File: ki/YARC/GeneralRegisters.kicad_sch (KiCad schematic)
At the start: 12 parts, among them U71 74LS670, U72 74LS670, U73 74LS157, U74 74LS670, U75 74LS670, U76 74LS157, U77 74LS670, U78 74LS670, U79 74LS157, U80 74LS670, U81 74LS670, U82 74LS157

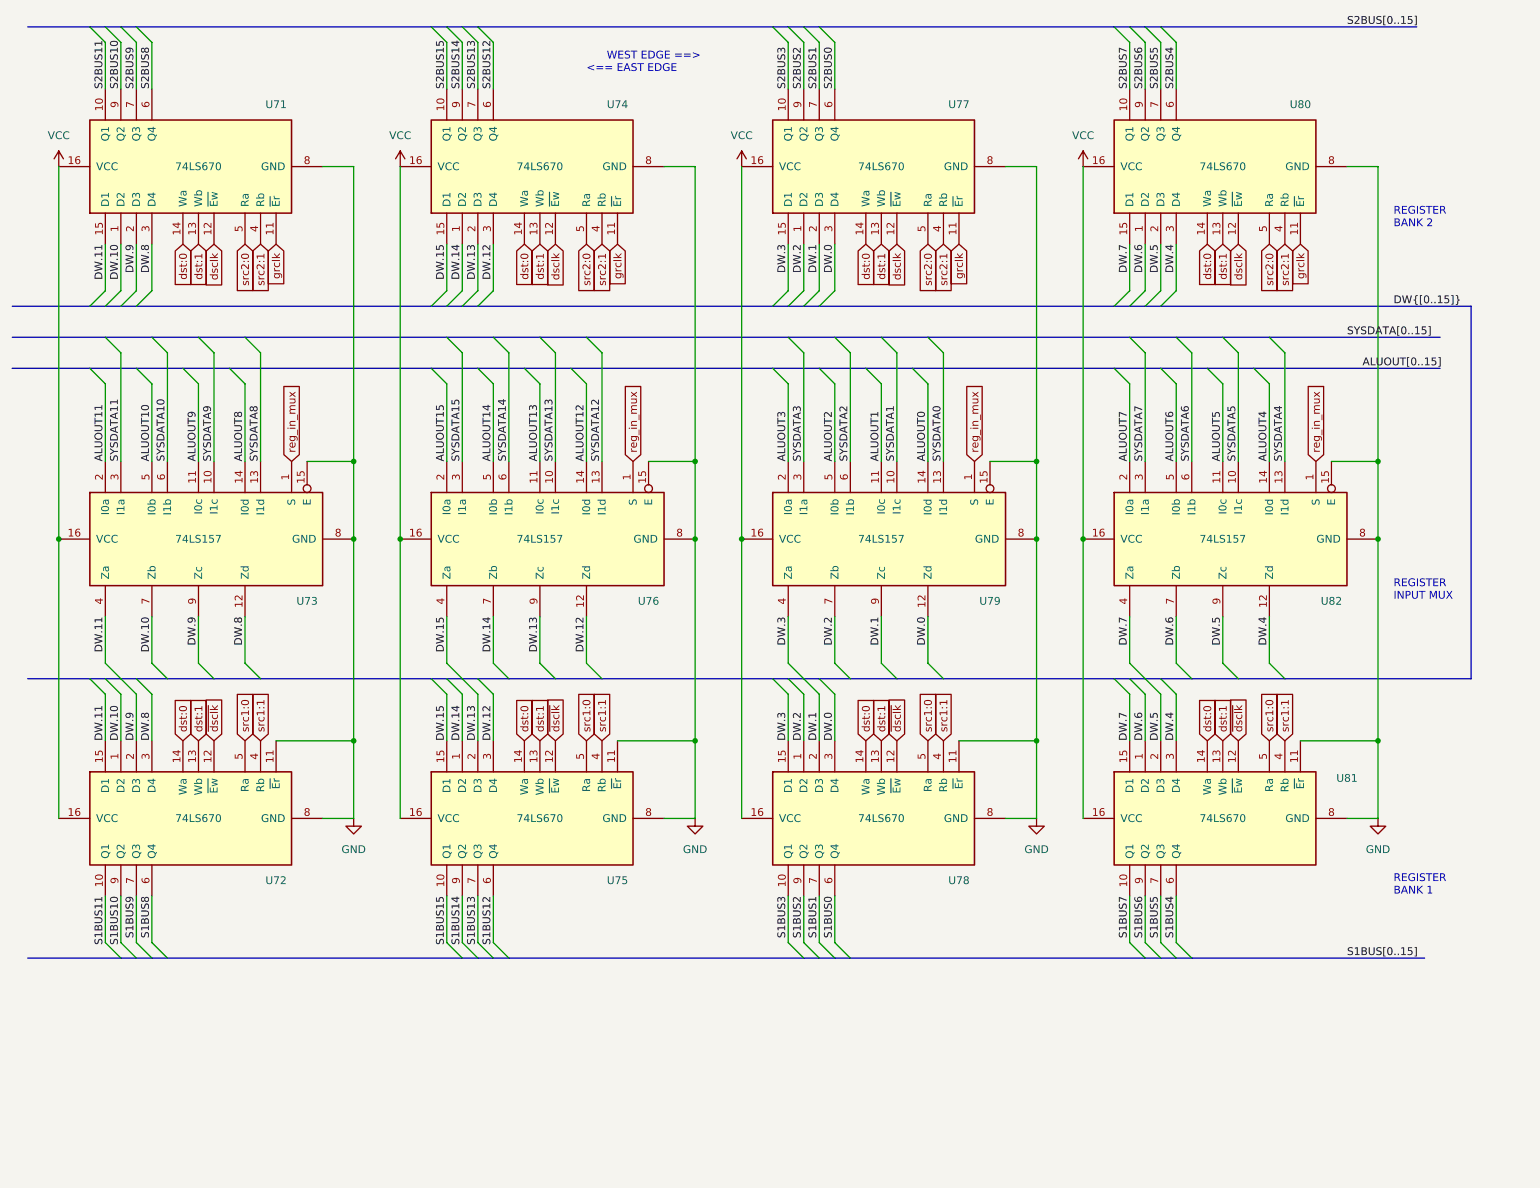
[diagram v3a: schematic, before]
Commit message: Add delay line for general register write signal. Minor corrections and cleanups.
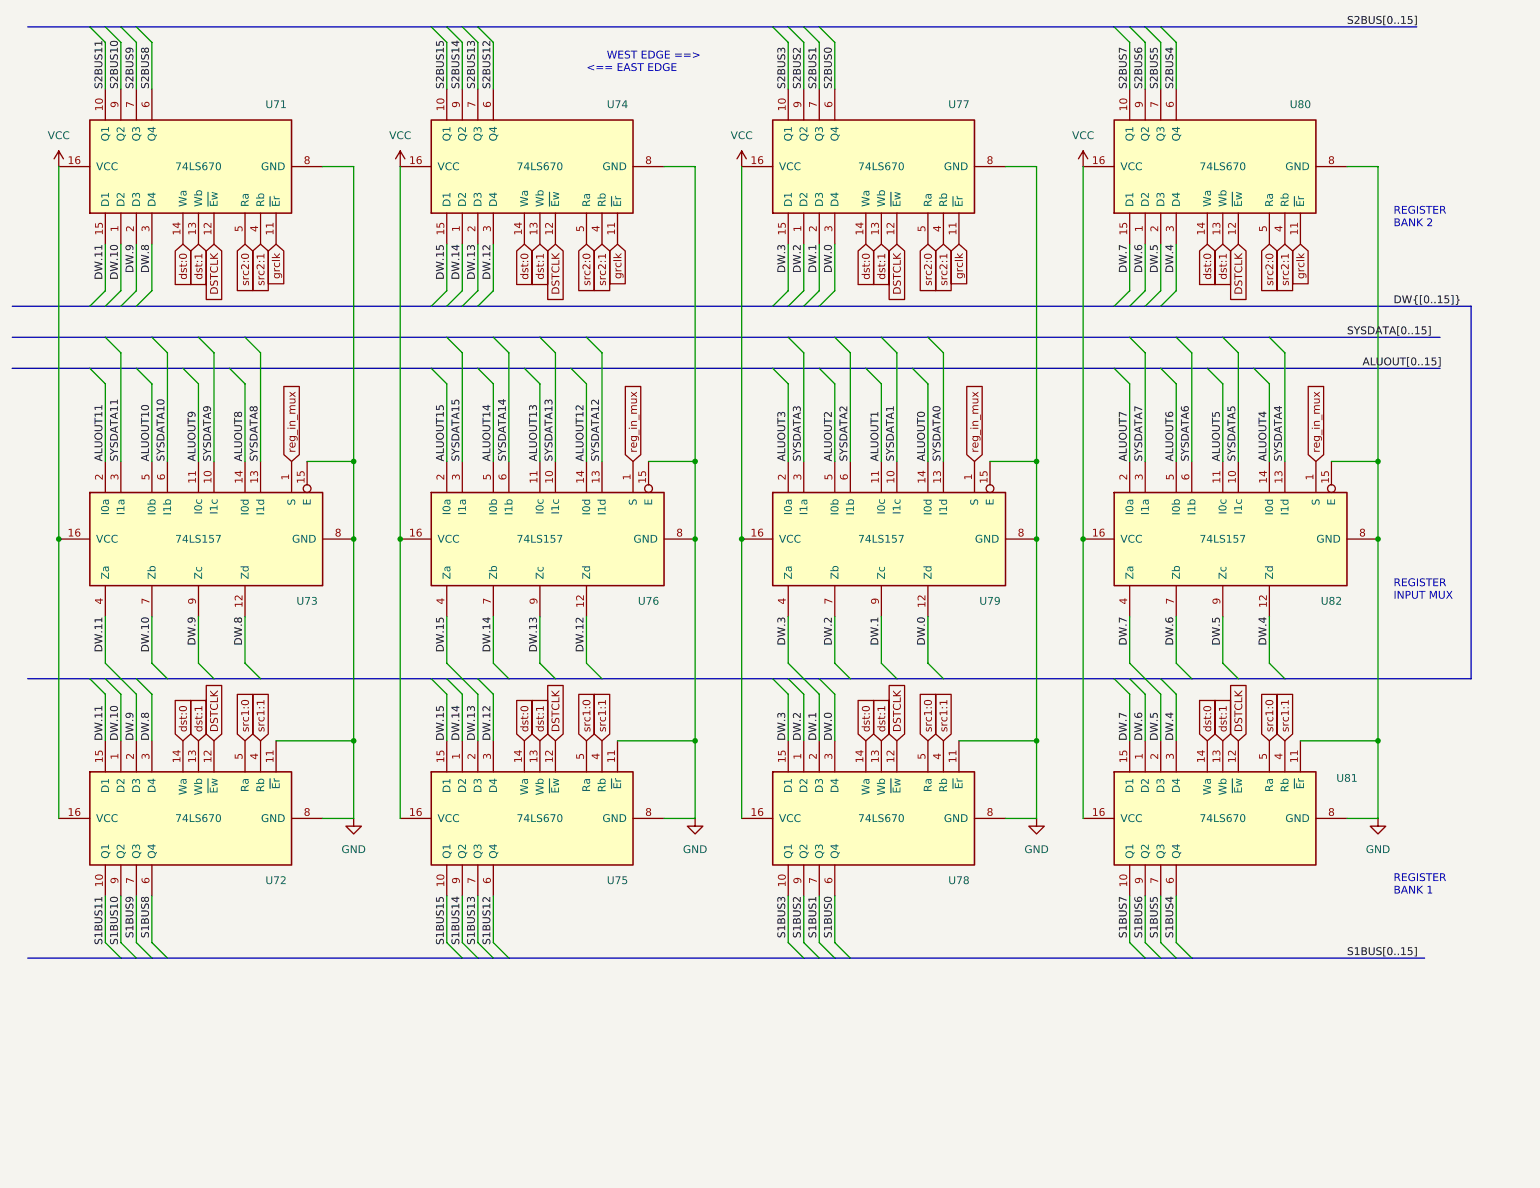
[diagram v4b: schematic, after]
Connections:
- net ~{dsclk} is gone; now on net DSTCLK: U72.12 (~{Ew}), U75.12 (~{Ew}), U78.12 (~{Ew}), U81.12 (~{Ew})
- net dsclk renamed DSTCLK
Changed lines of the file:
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@@
     )
   )
-  (global_label "~{dsclk}" (shape input) (at 104.14 132.08 90) (fields_autoplaced)
-    (effects (font (size 1.27 1.27)) (justify left))
-    (property "Intersheet References" "${INTERSHEET_REFS}" (id 0) (at 104.2194 124.7079 90)
+  (global_label "DSTCLK" (shape input) (at 104.14 132.08 90) (fields_autoplaced)
+    (effects (font (size 1.27 1.27)) (justify left))
+    (property "Intersheet References" "${INTERSHEET_REFS}" (id 0) (at 104.0606 122.6517 90)
       (effects (font (size 1.27 1.27)) (justify left) hide)
     )
@@
     )
   )
-  (global_label "dsclk" (shape input) (at 160.02 50.8 270) (fields_autoplaced)
-    (effects (font (size 1.27 1.27)) (justify right))
-    (property "Intersheet References" "${INTERSHEET_REFS}" (id 0) (at 159.9406 58.1721 90)
+  (global_label "DSTCLK" (shape input) (at 160.02 50.8 270) (fields_autoplaced)
+    (effects (font (size 1.27 1.27)) (justify right))
+    (property "Intersheet References" "${INTERSHEET_REFS}" (id 0) (at 159.9406 60.2283 90)
       (effects (font (size 1.27 1.27)) (justify right) hide)
     )
@@
     )
   )
-  (global_label "~{dsclk}" (shape input) (at 48.26 132.08 90) (fields_autoplaced)
-    (effects (font (size 1.27 1.27)) (justify left))
-    (property "Intersheet References" "${INTERSHEET_REFS}" (id 0) (at 48.3394 124.7079 90)
-      (effects (font (size 1.27 1.27)) (justify left) hide)
-    )
-  )
-  (global_label "dsclk" (shape input) (at 104.14 50.8 270) (fields_autoplaced)
-    (effects (font (size 1.27 1.27)) (justify right))
-    (property "Intersheet References" "${INTERSHEET_REFS}" (id 0) (at 104.0606 58.1721 90)
+  (global_label "DSTCLK" (shape input) (at 48.26 132.08 90) (fields_autoplaced)
+    (effects (font (size 1.27 1.27)) (justify left))
+    (property "Intersheet References" "${INTERSHEET_REFS}" (id 0) (at 48.1806 122.6517 90)
+      (effects (font (size 1.27 1.27)) (justify left) hide)
+    )
+  )
+  (global_label "DSTCLK" (shape input) (at 104.14 50.8 270) (fields_autoplaced)
+    (effects (font (size 1.27 1.27)) (justify right))
+    (property "Intersheet References" "${INTERSHEET_REFS}" (id 0) (at 104.0606 60.2283 90)
       (effects (font (size 1.27 1.27)) (justify right) hide)
     )
@@
     )
   )
-  (global_label "~{dsclk}" (shape input) (at 160.02 132.08 90) (fields_autoplaced)
-    (effects (font (size 1.27 1.27)) (justify left))
-    (property "Intersheet References" "${INTERSHEET_REFS}" (id 0) (at 160.0994 124.7079 90)
+  (global_label "DSTCLK" (shape input) (at 160.02 132.08 90) (fields_autoplaced)
+    (effects (font (size 1.27 1.27)) (justify left))
+    (property "Intersheet References" "${INTERSHEET_REFS}" (id 0) (at 159.9406 122.6517 90)
       (effects (font (size 1.27 1.27)) (justify left) hide)
     )
@@
     )
   )
-  (global_label "dsclk" (shape input) (at 215.9 50.8 270) (fields_autoplaced)
-    (effects (font (size 1.27 1.27)) (justify right))
-    (property "Intersheet References" "${INTERSHEET_REFS}" (id 0) (at 215.8206 58.1721 90)
+  (global_label "DSTCLK" (shape input) (at 215.9 50.8 270) (fields_autoplaced)
+    (effects (font (size 1.27 1.27)) (justify right))
+    (property "Intersheet References" "${INTERSHEET_REFS}" (id 0) (at 215.8206 60.2283 90)
       (effects (font (size 1.27 1.27)) (justify right) hide)
     )
@@
     )
   )
-  (global_label "dsclk" (shape input) (at 48.26 50.8 270) (fields_autoplaced)
-    (effects (font (size 1.27 1.27)) (justify right))
-    (property "Intersheet References" "${INTERSHEET_REFS}" (id 0) (at 48.1806 58.1721 90)
+  (global_label "DSTCLK" (shape input) (at 48.26 50.8 270) (fields_autoplaced)
+    (effects (font (size 1.27 1.27)) (justify right))
+    (property "Intersheet References" "${INTERSHEET_REFS}" (id 0) (at 48.1806 60.2283 90)
       (effects (font (size 1.27 1.27)) (justify right) hide)
     )
@@
     )
   )
-  (global_label "~{dsclk}" (shape input) (at 215.9 132.08 90) (fields_autoplaced)
-    (effects (font (size 1.27 1.27)) (justify left))
-    (property "Intersheet References" "${INTERSHEET_REFS}" (id 0) (at 215.9794 124.7079 90)
-      (effects (font (size 1.27 1.27)) (justify left) hide)
-    )
+  (global_label "DSTCLK" (shape input) (at 215.9 132.08 90) (fields_autoplaced)
+    (effects (font (size 1.27 1.27)) (justify left))
+    (property "Intersheet References" "${INTERSHEET_REFS}" (id 0) (at 215.8206 122.6517 90)
+      (effects (font (size 1.27 1.27)) (justify left) hide)
+    )

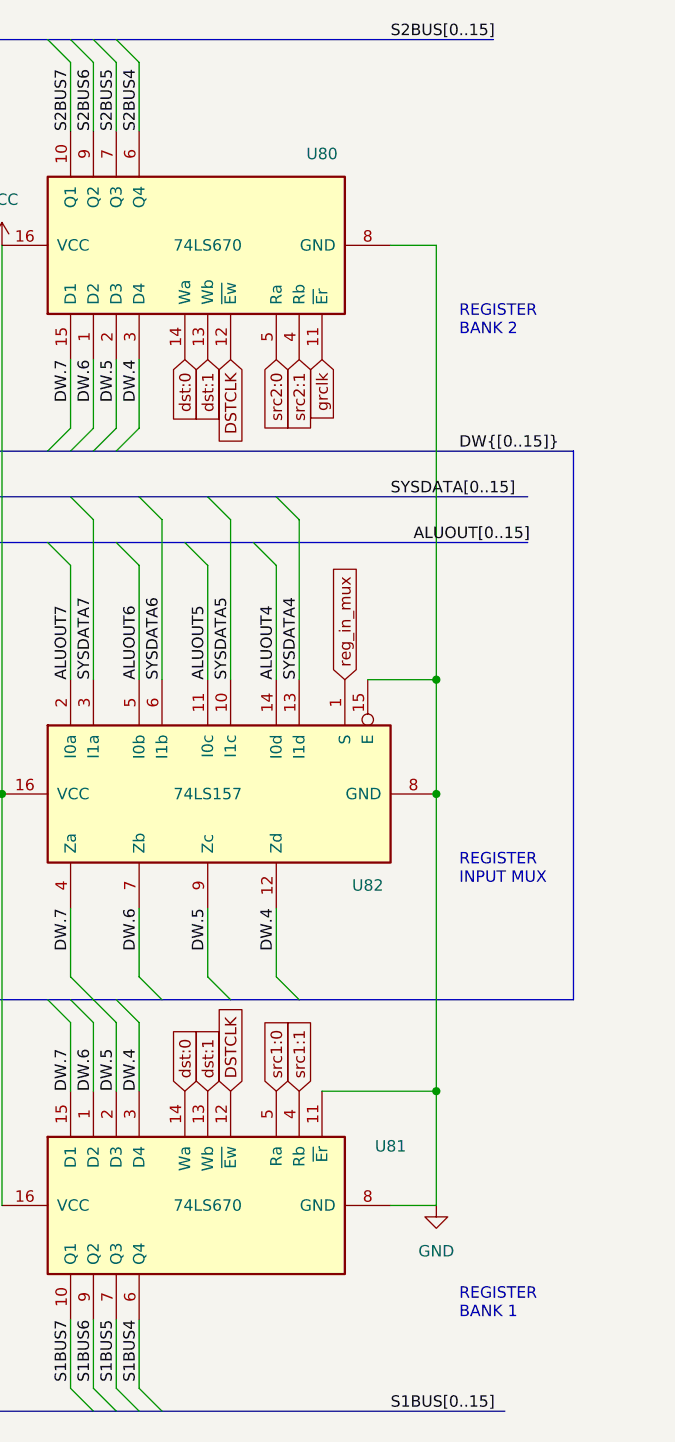
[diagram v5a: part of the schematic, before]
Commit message: Removed about 2/3 of 2300+ errors from the ERC
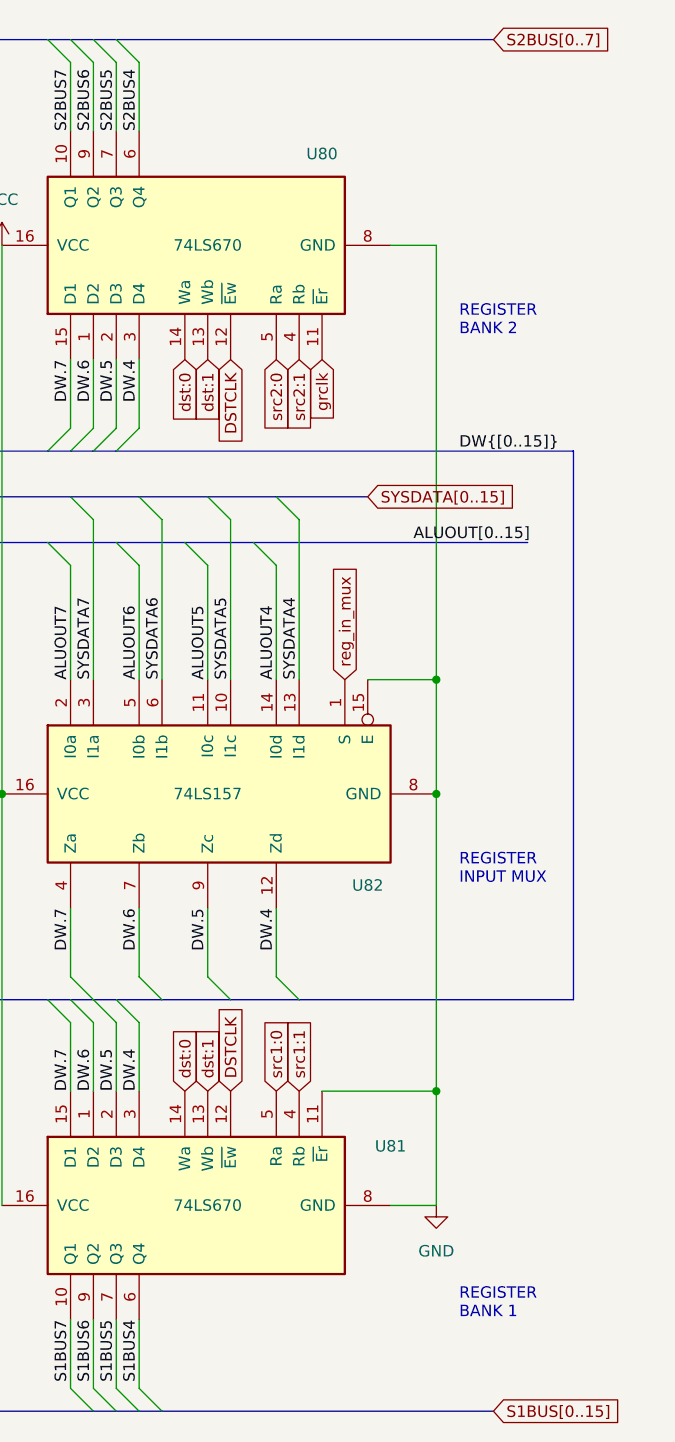
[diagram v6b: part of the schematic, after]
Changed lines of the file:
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@@
     (stroke (width 0) (type default))
   )
-  (bus (pts (xy 208.28 167.64) (xy 246.38 167.64))
+  (bus (pts (xy 208.28 167.64) (xy 245.11 167.64))
     (stroke (width 0) (type default))
   )
@@
     (stroke (width 0) (type default))
   )
-  (bus (pts (xy 220.98 66.04) (xy 248.92 66.04))
+  (bus (pts (xy 220.98 66.04) (xy 231.14 66.04))
     (stroke (width 0) (type default))
   )
@@
     (effects (font (size 1.27 1.27)) (justify left bottom))
   )
-  (label "S2BUS[0..15]" (at 233.68 15.24 0) (fields_autoplaced)
-    (effects (font (size 1.27 1.27)) (justify left bottom))
-  )
   (label "ALUOUT0" (at 165.1 86.36 90) (fields_autoplaced)
     (effects (font (size 1.27 1.27)) (justify left bottom))
@@
     (effects (font (size 1.27 1.27)) (justify right bottom))
   )
-  (label "SYSDATA[0..15]" (at 233.68 66.04 0) (fields_autoplaced)
-    (effects (font (size 1.27 1.27)) (justify left bottom))
-  )
   (label "DW.2" (at 144.78 50.8 270) (fields_autoplaced)
     (effects (font (size 1.27 1.27)) (justify right bottom))
@@
     (effects (font (size 1.27 1.27)) (justify left bottom))
   )
-  (label "S1BUS[0..15]" (at 233.68 167.64 0) (fields_autoplaced)
-    (effects (font (size 1.27 1.27)) (justify left bottom))
-  )
   (label "DW.8" (at 53.34 111.76 270) (fields_autoplaced)
     (effects (font (size 1.27 1.27)) (justify right bottom))
@@
     (effects (font (size 1.27 1.27)) (justify left bottom))
   )
+  (global_label "S2BUS[0..7]" (shape input) (at 245.11 15.24 0) (fields_autoplaced)
+    (effects (font (size 1.27 1.27)) (justify left))
+    (property "Intersheetrefs" "${INTERSHEET_REFS}" (at 259.6462 15.24 0)
+      (effects (font (size 1.27 1.27)) (justify left) hide)
+    )
+  )
   (global_label "dst:0" (shape input) (at 210.82 132.08 90) (fields_autoplaced)
     (effects (font (size 1.27 1.27)) (justify left))
@@
     )
   )
+  (global_label "SYSDATA[0..15]" (shape input) (at 231.14 66.04 0) (fields_autoplaced)
+    (effects (font (size 1.27 1.27)) (justify left))
+    (property "Intersheetrefs" "${INTERSHEET_REFS}" (at 248.5791 66.04 0)
+      (effects (font (size 1.27 1.27)) (justify left) hide)
+    )
+  )
   (global_label "src2:0" (shape input) (at 220.98 50.8 270) (fields_autoplaced)
     (effects (font (size 1.27 1.27)) (justify right))
@@
     )
   )
+  (global_label "S1BUS[0..15]" (shape input) (at 245.11 167.64 0) (fields_autoplaced)
+    (effects (font (size 1.27 1.27)) (justify left))
+    (property "Intersheetrefs" "${INTERSHEET_REFS}" (at 260.8557 167.64 0)
+      (effects (font (size 1.27 1.27)) (justify left) hide)
+    )
+  )
